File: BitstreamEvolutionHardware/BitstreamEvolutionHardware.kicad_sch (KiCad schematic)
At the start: 61 parts, among them J1 PPPC101LFBN-RC, J10 61300211121, J11 61300211121, J12 61300211121, J13 61300211121, J14 61300211121, J15 61300211121, J16 61300211121, J17 61300211121, J18 61300211121, J19 61300211121, J2 PPPC101LFBN-RC, J20 61300211121, J21 61300211121, J22 61300211121, J23 61300211121, J24 61300211121, J25 61300211121, J26 61300211121, J27 61300211121, J28 61300211121, J29 61300211121, J3 61300211121, J30 61300211121, J31 61300211121, J32 61300211121, J33 61300211121, J34 61300211121, J35 61300211121, J36 61300211121, J37 61300211121, J38 61300211121, J39 61300211121, J4 61300211121, J5 61300211121, J6 61300211121, J7 61300211121, J8 61300211121, J9 61300211121, U1 ADS7828, U2 ADS7828, U3 PPTC151LFBN-RC, U4 PPTC151LFBN-RC, U5 MAX5820MEUA+, U6 MAX5820MEUA+, U7 AD9833BRMZ, Y1 XRCGB25M000F3M04R0

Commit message: Backup
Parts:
- removed R10: 2K, Resistor_SMD:R_0201_0603Metric, symbol Device:R_Small
- removed U5, U6: MAX5820MEUA+, footprints:MAX5820MEUA&plus_, symbol MAXDAC:MAX5820MEUA+
- removed U7: AD9833BRMZ, SOP50P490X110-10N, symbol AD9833BRMZ:AD9833BRMZ
- removed Y1: XRCGB25M000F3M04R0, footprints:OSC_XRCGB25M000F3M04R0, symbol XRCGB25M000F3M04R0:XRCGB25M000F3M04R0
- added C3, C4, C7: 10uF, Capacitor_SMD:C_0805_2012Metric, symbol Device:C_Small
- added C5, C6: 0.47uF, Resistor_SMD:R_0805_2012Metric, symbol Device:C_Small
- added C8: 0.1uF, Capacitor_SMD:C_0805_2012Metric, symbol Device:C_Small
- added H1, H2, H3, H4: MountingHole, gld:MountingHole_3.2mm_M3, symbol Mechanical:MountingHole
- added J40, J41, J42, J43, J44, J45: 61300211121, 61300211121, symbol 61300211121:61300211121
- added Q1, Q2: BSS138, Package_TO_SOT_SMD:SOT-23, symbol Transistor_FET:BSS138
- added R13, R14: 10K, Resistor_SMD:R_0805_2012Metric, symbol Device:R_Small
- added R15, R16, R17, R18: 0, Resistor_SMD:R_0805_2012Metric, symbol Device:R_Small
- added R19, R20, R21, R22: 0, Resistor_SMD:R_0201_0603Metric, symbol Device:R_Small
- added U5: MCP4728, Package_SO:MSOP-10_3x3mm_P0.5mm, symbol Analog_DAC:MCP4728
- added U7: RT9193-33GB, SOT94P279X129-5N, symbol RT9193-33GB:RT9193-33GB
- added U8: Si5351A-B-GT, Package_SO:MSOP-10_3x3mm_P0.5mm, symbol Oscillator:Si5351A-B-GT
- added Y1: ABM8G-25.000MHZ-4Y-T3, XTAL_ABM8G-25.000MHZ-4Y-T3, symbol ABM8G-25.000MHZ-4Y-T3:ABM8G-25.000MHZ-4Y-T3
- C1: value C_Small -> 10uF; footprint (none) -> Capacitor_SMD:C_0805_2012Metric
- R1, R2, R3: footprint Resistor_SMD:R_0201_0603Metric -> Resistor_SMD:R_0805_2012Metric
- R11, R12: value 2K -> 10K; footprint Resistor_SMD:R_0201_0603Metric -> Resistor_SMD:R_0805_2012Metric
- R7, R8, R9: value 2K -> 4.7K; footprint Resistor_SMD:R_0201_0603Metric -> Resistor_SMD:R_0805_2012Metric
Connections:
- net ADC_B_Channel_0: now also U1.8 (CH7); no longer U1.1 (CH0)
- net ADC_B_Channel_1: now also U1.7 (CH6); no longer U1.2 (CH1)
- net ADC_B_Channel_2: now also U1.6 (CH5); no longer U1.3 (CH2)
- net ADC_B_Channel_3: now also U1.5 (CH4); no longer U1.4 (CH3)
- net ADC_B_Channel_4: now also U1.4 (CH3); no longer U1.5 (CH4)
- net ADC_B_Channel_5: now also U1.3 (CH2); no longer U1.6 (CH5)
- net ADC_B_Channel_6: now also U1.2 (CH1); no longer U1.7 (CH6)
- net ADC_B_Channel_7: now also U1.1 (CH0); no longer U1.8 (CH7)
- net Arduino_+3.3V: now also R17.1, R18.1, R19.1, R21.1; no longer U1.12 (A0), U1.13 (A1)
- net Arduino_+5V: now also R8.1, R9.1, C3.1, C7.1, C8.2, R13.2, R14.2, U5.1 (VDD), U7.1 (VIN), U7.3 (EN)
- net Arduino_AREF: now also J45.1
- net Arduino_SCL: now also R8.2, Q1.3 (D), R14.1, U5.3 (SDA); no longer R12.2, R7.1, R9.1
- net Arduino_SDA: now also R9.2, Q2.3 (D), R13.1, U5.2 (SCL); no longer R11.1, R8.1
- net GND: now also C3.2, C4.2, C5.1, C6.2, C7.2, C8.1, J40.2, J41.2, J45.2, R15.2, R16.2, R20.2, R22.2, U5.10 (VSS), U7.2 (GND), U8.8 (GND), Y1.2 (GND), Y1.4 (GND); no longer U2.12 (A0), U2.13 (A1)
- net at J36.1: now also U5.6 (VOUTA)
- net at J36.2: now also J37.2, J42.2, J43.2
- net at J37.1: now also U5.7 (VOUTB)
- net at R7.2: now also U5.4 (~{LDAC})
- net Generator_VDD: now reaches R11.2
- net Generator_VDD: now also R12.2, C4.1, C5.2, C6.1, Q1.1 (G), Q2.1 (G), U7.5 (VOUT), U8.1 (VDD), U8.7 (VDDO)
- net at J38.1: now also U8.10 (CLK0)
- net Generator_3V_SDA: now reaches R12.1
- net Generator_3V_SDA: now also Q2.2 (S), U8.5 (SDA)
- new net: J40.1, U8.6 (CLK2)
- new net: R19.2, R21.2, R22.1, U1.12 (A0)
- new net: J43.1, U5.9 (VOUTD)
- new net: R20.1, U1.13 (A1)
- new net: J41.1, U8.9 (CLK1)
- new net: J42.1, U5.8 (VOUTC)
- new net: J44.1, U5.5 (RDY/~{BSY})
- new net: J44.2, R7.1
- new net: R16.1, R17.2, U2.13 (A1)
- new net: R15.1, R18.2, U2.12 (A0)
- new net: U8.2 (XA), Y1.1
- new net: U8.3 (XB), Y1.3
- new net Generator_3V_SCL: Q1.2 (S), R11.1, U8.4 (SCL)
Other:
- note added: "0x60 I2C Address"
- note added: "Clock Generator Section"
- note added: "DAC Section"
- note added: "Flipped for Ease of Routing"
- note added: "https://learn.adafruit.com/adafruit-mcp4728-i2c-quad-dac?view=all"
- note added: "https://www.adafruit.com/product/2045"
- note removed: "Waveform Generator"
- moved on the sheet: J10, J11, J12, J13, J14, J15, J16, J17, J18, J19, J20, J21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

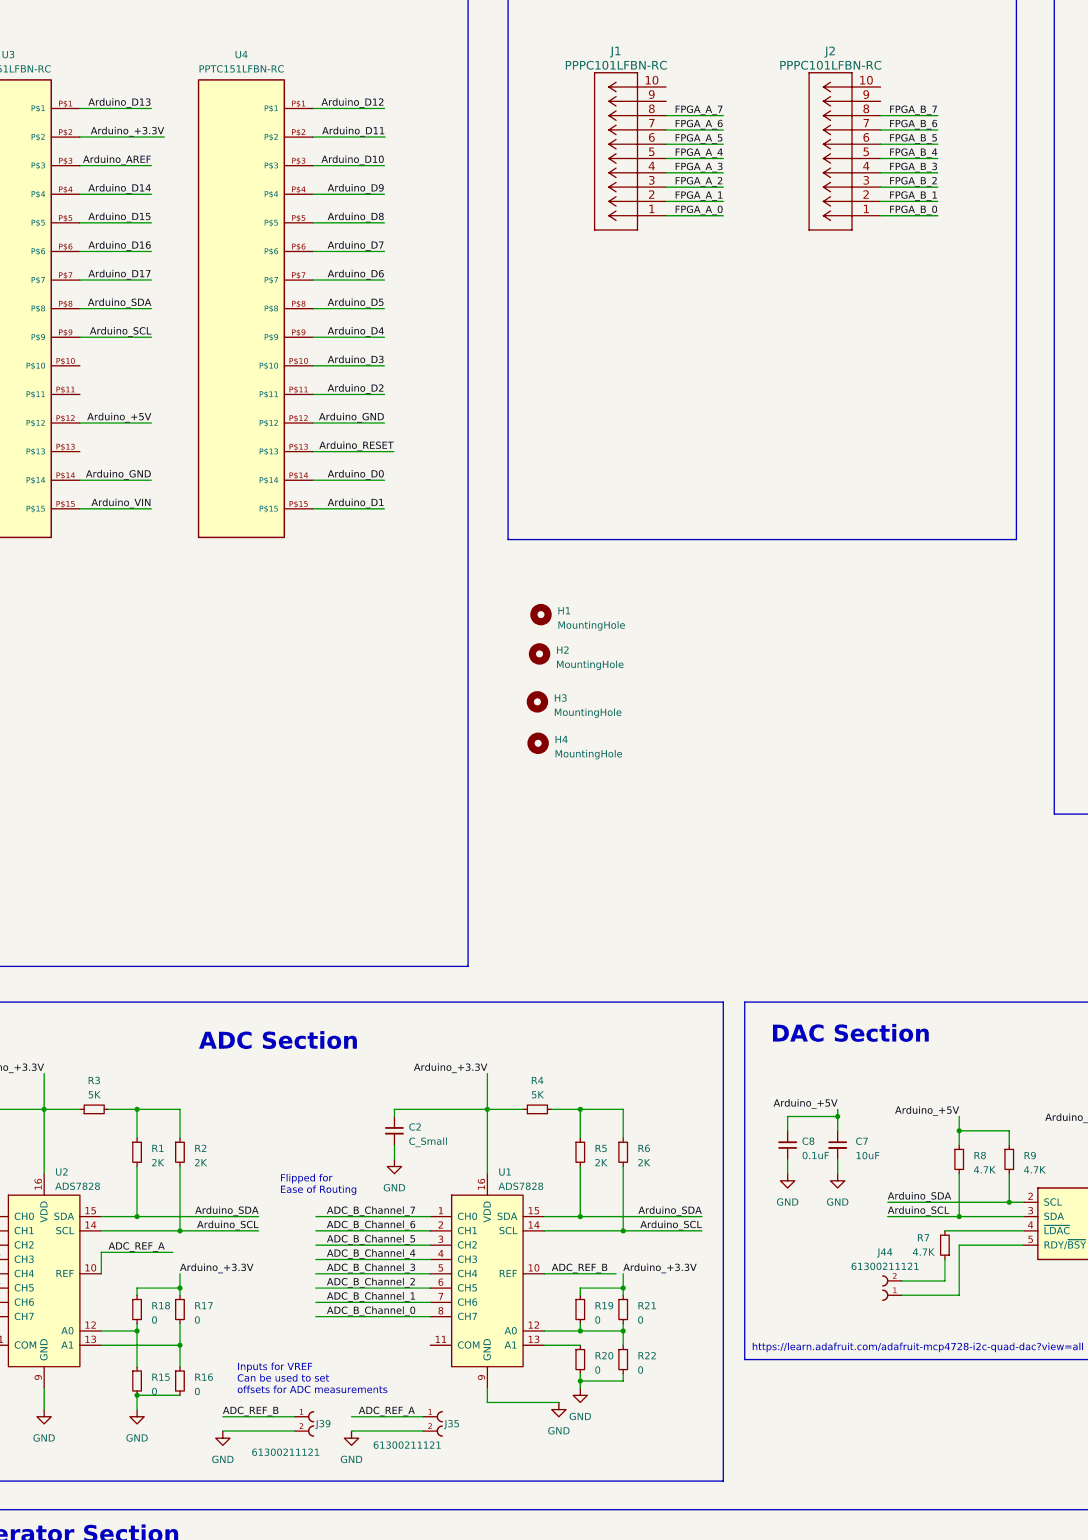
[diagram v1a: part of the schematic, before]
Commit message: Almost Done with Routing, need to route power and I2C Lines
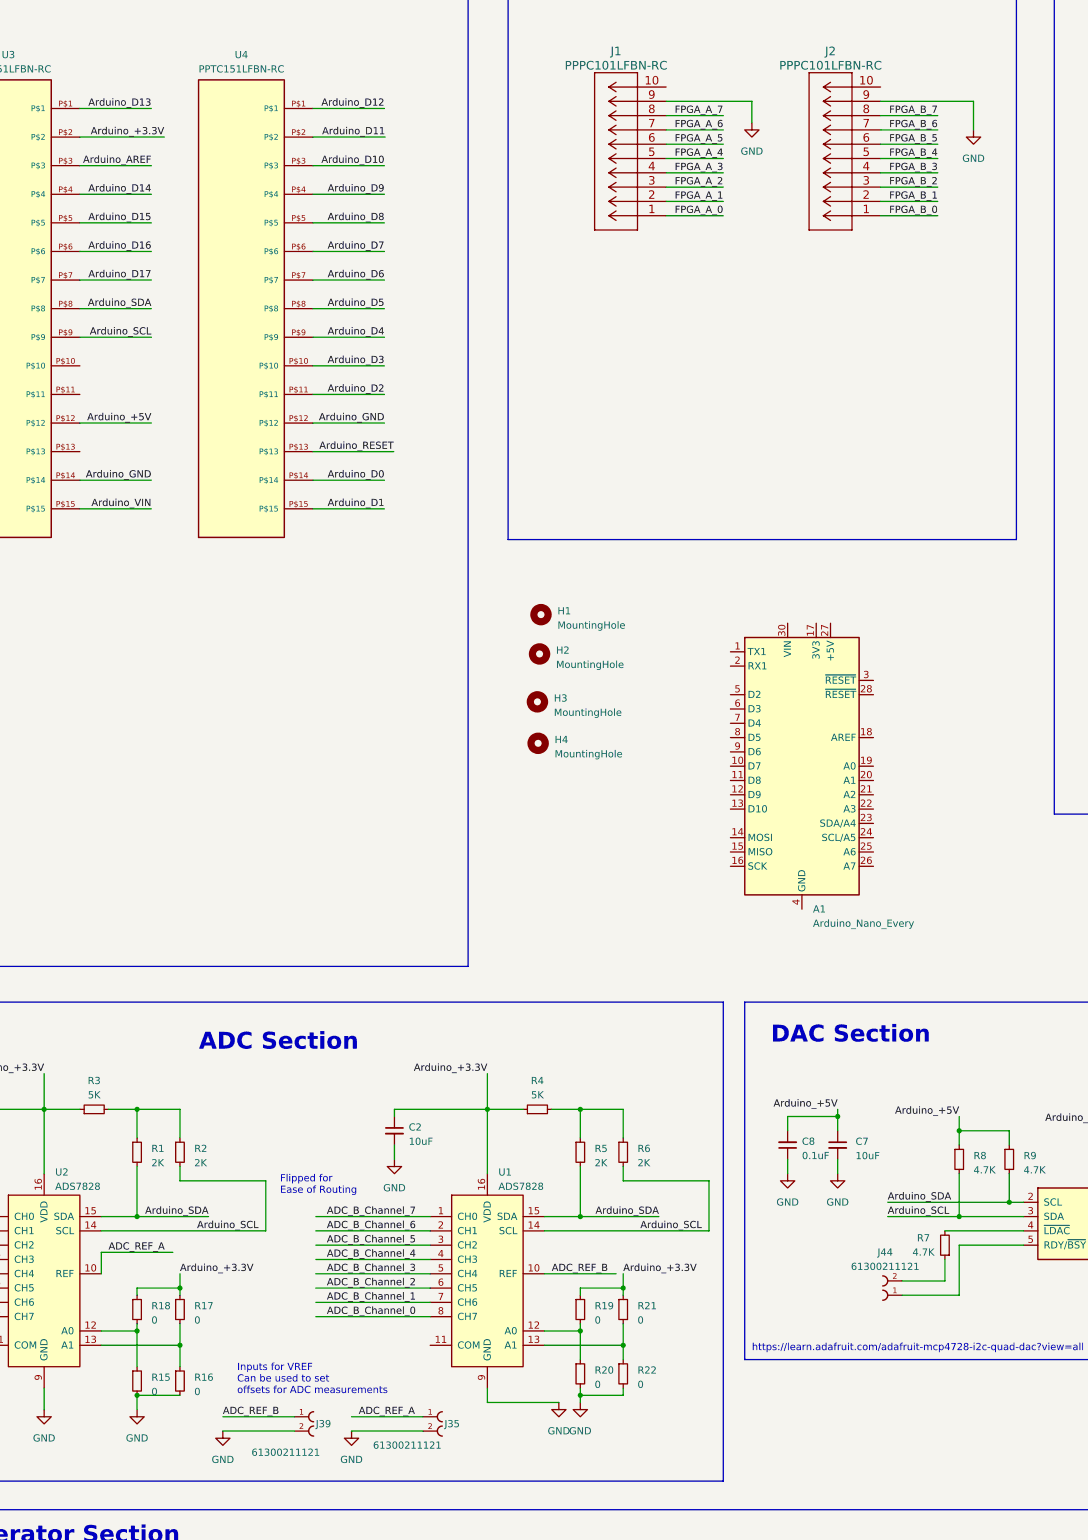
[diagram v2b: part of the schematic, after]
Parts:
- added A1: Arduino_Nano_Every, Module:Arduino_Nano, symbol MCU_Module:Arduino_Nano_Every
- C2: value C_Small -> 10uF; footprint (none) -> Resistor_SMD:R_0805_2012Metric
- R19, R20, R21, R22, R4, R5, R6: footprint Resistor_SMD:R_0201_0603Metric -> Resistor_SMD:R_0805_2012Metric
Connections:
- net GND: now also J1.9, J2.9
- net at R21.2, R22.1: now also U1.13 (A1); no longer R19.2, U1.12 (A0)
- net at R20.1: now also R19.2, U1.12 (A0); no longer U1.13 (A1)
- new net: A1.29 (GND), A1.4 (GND)
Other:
- moved on the sheet: R20, R22
